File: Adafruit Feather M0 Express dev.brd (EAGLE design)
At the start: 50.8 x 22.9 mm, 41 parts, among them J2 AVR_SPI_PROG_3X2PTH, SW1 SPST_TACT-KMR2, U1 2MB Flash, U2 AP2112-3.3, U3 MCP73831T-2ACI/OT, X1 JSTPH, X2 32.768, X3 microUSB, X4 2x5 0.05" SWD

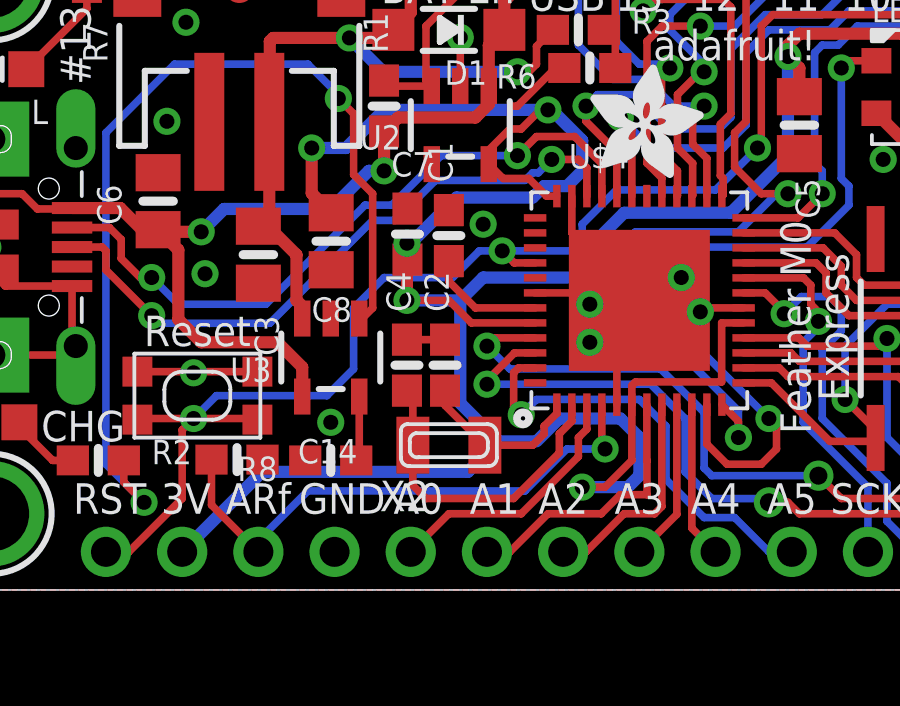
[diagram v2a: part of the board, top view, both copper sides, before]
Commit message: last bad overlap fixed! Still unsure about the bottom layer groundplane under the +3v3 end of C7
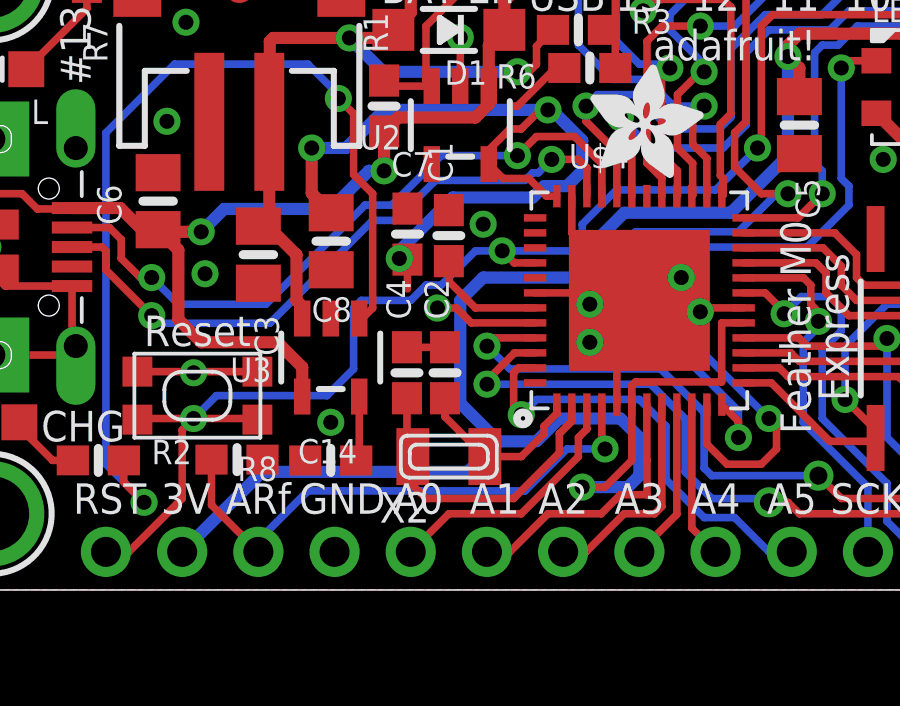
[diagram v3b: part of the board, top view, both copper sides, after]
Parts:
- moved X2 0.38 mm to (17.8, 4.45)
- moved C2 0.25 mm to (17.7, 7.24)
- moved C4 0.25 mm to (16.4, 7.24)
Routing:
- net +3V3: track 150.3 -> 145.9 mm
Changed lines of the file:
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@@
 <attribute name="VALUE" x="18.161" y="10.795" size="0.8128" layer="27" font="vector" ratio="10" rot="R90"/>
 </element>
-<element name="C2" library="microbuilder" package="0603-NO" value="22pF" x="17.653" y="7.493" smashed="yes" rot="R90">
-<attribute name="NAME" x="17.78" y="9.271" size="0.8128" layer="25" font="vector" ratio="18" rot="R90"/>
-<attribute name="VALUE" x="18.034" y="6.477" size="0.8128" layer="27" font="vector" ratio="10" rot="R90"/>
-</element>
-<element name="C4" library="microbuilder" package="0603-NO" value="22pF" x="16.383" y="7.493" smashed="yes" rot="R90">
-<attribute name="NAME" x="16.51" y="9.271" size="0.8128" layer="25" font="vector" ratio="18" rot="R90"/>
-<attribute name="VALUE" x="16.891" y="6.35" size="0.8128" layer="27" font="vector" ratio="10" rot="R90"/>
-</element>
-<element name="X2" library="adafruit2" package="XTAL3215" value="32.768" x="17.78" y="4.826" smashed="yes">
-<attribute name="NAME" x="15.48" y="2.626" size="1.016" layer="25" font="vector"/>
-<attribute name="VALUE" x="15.942" y="4.502" size="0.8128" layer="27" font="vector"/>
+<element name="C2" library="microbuilder" package="0603-NO" value="22pF" x="17.653" y="7.239" smashed="yes" rot="R90">
+<attribute name="NAME" x="17.78" y="9.017" size="0.8128" layer="25" font="vector" ratio="18" rot="R90"/>
+<attribute name="VALUE" x="18.034" y="6.223" size="0.8128" layer="27" font="vector" ratio="10" rot="R90"/>
+</element>
+<element name="C4" library="microbuilder" package="0603-NO" value="22pF" x="16.383" y="7.239" smashed="yes" rot="R90">
+<attribute name="NAME" x="16.51" y="9.017" size="0.8128" layer="25" font="vector" ratio="18" rot="R90"/>
+<attribute name="VALUE" x="16.891" y="6.096" size="0.8128" layer="27" font="vector" ratio="10" rot="R90"/>
+</element>
+<element name="X2" library="adafruit2" package="XTAL3215" value="32.768" x="17.78" y="4.445" smashed="yes">
+<attribute name="NAME" x="15.48" y="2.245" size="1.016" layer="25" font="vector"/>
+<attribute name="VALUE" x="15.942" y="4.121" size="0.8128" layer="27" font="vector"/>
 </element>
 <element name="C5" library="microbuilder" package="0805-NO" value="10uF" x="29.464" y="15.494" smashed="yes" rot="R270">
@@
 <wire x1="23.88" y1="9.902" x2="24.13" y2="9.652" width="0.254" layer="1"/>
 <wire x1="23.38" y1="6.177" x2="23.38" y2="8.902" width="0.254" layer="1"/>
-<wire x1="17.653" y1="8.343" x2="16.383" y2="8.343" width="0.254" layer="1"/>
+<wire x1="17.653" y1="8.089" x2="16.383" y2="8.089" width="0.254" layer="1"/>
 <via x="9.271" y="7.239" extent="1-16" drill="0.5"/>
 <via x="18.923" y="12.192" extent="1-16" drill="0.5"/>
@@
 <wire x1="22.987" y1="3.429" x2="22.225" y2="3.429" width="0.254" layer="1"/>
 <via x="22.225" y="3.429" extent="1-16" drill="0.5"/>
-<via x="16.383" y="9.652" extent="1-16" drill="0.5"/>
+<via x="17.399" y="9.398" extent="1-16" drill="0.5"/>
 <wire x1="21.463" y1="5.715" x2="23.499" y2="5.715" width="0.4064" layer="16"/>
 <wire x1="23.499" y1="5.715" x2="24.13" y2="5.084" width="0.4064" layer="16"/>
@@
 <wire x1="21.209" y1="16.002" x2="22.225" y2="14.986" width="0.4064" layer="16"/>
 <wire x1="16.4" y1="10.0351" x2="16.4" y2="11.012" width="0.254" layer="1"/>
-<wire x1="18.161" y1="9.652" x2="16.51" y2="9.652" width="0.4064" layer="16"/>
 <wire x1="27.605" y1="8.902" x2="26.8732" y2="8.902" width="0.254" layer="1"/>
 <wire x1="26.8732" y1="8.902" x2="26.8732" y2="6.9342" width="0.254" layer="1"/>
@@
 <wire x1="20.193" y1="15.367" x2="20.828" y2="16.002" width="0.254" layer="1"/>
 <wire x1="20.828" y1="16.002" x2="21.082" y2="16.002" width="0.254" layer="1"/>
-<wire x1="16.51" y1="9.652" x2="16.383" y2="9.525" width="0.4064" layer="16"/>
-<wire x1="16.383" y1="9.525" x2="16.383" y2="9.652" width="0.4064" layer="16"/>
-<wire x1="16.383" y1="9.652" x2="16.383" y2="10.995" width="0.4064" layer="1"/>
 <wire x1="27.178" y1="12.573" x2="23.622" y2="12.573" width="0.4064" layer="16"/>
 <wire x1="27.178" y1="12.573" x2="29.083" y2="14.478" width="0.4064" layer="16"/>
@@
 <wire x1="20.447" y1="13.716" x2="19.5889" y2="13.716" width="0.254" layer="1"/>
 <wire x1="19.5889" y1="13.716" x2="19.111" y2="14.1939" width="0.254" layer="1"/>
-<wire x1="20.574" y1="13.081" x2="20.955" y2="13.462" width="0.4064" layer="16"/>
+<wire x1="20.955" y1="13.462" x2="20.574" y2="13.081" width="0.4064" layer="16"/>
 <wire x1="21.717" y1="13.462" x2="20.955" y2="13.462" width="0.4064" layer="16"/>
-<wire x1="16.4" y1="11.012" x2="16.4" y2="11.54" width="0.4064" layer="1"/>
-<wire x1="16.4" y1="11.54" x2="16.383" y2="11.557" width="0.4064" layer="1"/>
-<via x="16.383" y="11.557" extent="1-16" drill="0.5"/>
-<wire x1="16.383" y1="11.557" x2="16.51" y2="11.557" width="0.4064" layer="16"/>
-<wire x1="16.51" y1="11.557" x2="18.034" y2="13.081" width="0.4064" layer="16"/>
-<wire x1="18.034" y1="13.081" x2="20.574" y2="13.081" width="0.4064" layer="16"/>
+<via x="16.129" y="11.049" extent="1-16" drill="0.5"/>
+<wire x1="16.129" y1="11.303" x2="16.129" y2="11.049" width="0.4064" layer="16"/>
 <wire x1="22.606" y1="10.414" x2="18.923" y2="10.414" width="0.4064" layer="16"/>
 <wire x1="18.923" y1="10.414" x2="18.161" y2="9.652" width="0.4064" layer="16"/>
 <wire x1="20.655" y1="8.902" x2="18.53" y2="8.902" width="0.254" layer="1"/>
-<wire x1="18.53" y1="8.902" x2="17.78" y2="9.652" width="0.254" layer="1"/>
-<wire x1="17.78" y1="9.652" x2="16.383" y2="9.652" width="0.254" layer="1"/>
+<wire x1="18.53" y1="8.902" x2="18.034" y2="9.398" width="0.254" layer="1"/>
+<wire x1="18.034" y1="9.398" x2="17.399" y2="9.398" width="0.254" layer="1"/>
 <contactref element="X4" pad="1"/>
 <contactref element="J2" pad="2"/>
@@
 <wire x1="29.464" y1="17.399" x2="29.464" y2="16.444" width="0.4064" layer="1"/>
 <contactref element="R4" pad="2"/>
+<wire x1="17.907" y1="13.081" x2="16.129" y2="11.303" width="0.4064" layer="16"/>
+<wire x1="20.574" y1="13.081" x2="17.907" y2="13.081" width="0.4064" layer="16"/>
 <wire x1="42.418" y1="4.191" x2="42.418" y2="4.003" width="0" layer="19" extent="1-1"/>
 <wire x1="20.701" y1="4.953" x2="20.574" y2="4.953" width="0" layer="19" extent="16-16"/>
+<wire x1="18.034" y1="9.398" x2="18.161" y2="9.652" width="0" layer="19" extent="1-16"/>
+<wire x1="16.4" y1="10.0351" x2="17.399" y2="9.398" width="0" layer="19" extent="1-1"/>
+<wire x1="16.129" y1="11.049" x2="16.4" y2="11.012" width="0" layer="19" extent="1-1"/>
 </signal>
 <signal name="VBUS">
@@
 <wire x1="22.225" y1="12.192" x2="22.225" y2="11.303" width="0.254" layer="16"/>
 <wire x1="22.225" y1="11.303" x2="19.558" y2="11.303" width="0.254" layer="16"/>
-<wire x1="17.907" y1="10.414" x2="15.621" y2="10.414" width="0.254" layer="16"/>
-<wire x1="15.621" y1="10.414" x2="14.605" y2="9.398" width="0.254" layer="16"/>
+<wire x1="14.605" y1="9.398" x2="14.859" y2="9.652" width="0.254" layer="16"/>
 <wire x1="28.067" y1="14.732" x2="26.67" y2="13.335" width="0.254" layer="16"/>
 <via x="28.067" y="14.732" extent="1-16" drill="0.5"/>
@@
 <wire x1="23.368" y1="13.335" x2="22.225" y2="12.192" width="0.254" layer="16"/>
 <wire x1="26.67" y1="13.335" x2="23.368" y2="13.335" width="0.254" layer="16"/>
-<wire x1="18.796" y1="11.303" x2="17.907" y2="10.414" width="0.254" layer="16"/>
-<wire x1="19.558" y1="11.303" x2="18.796" y2="11.303" width="0.254" layer="16"/>
 <wire x1="44.205" y1="13.97" x2="44.205" y2="16.882" width="0.254" layer="1"/>
 <wire x1="44.205" y1="16.882" x2="43.307" y2="17.78" width="0.254" layer="1"/>
+<wire x1="17.526" y1="10.16" x2="18.669" y2="11.303" width="0.254" layer="16"/>
+<wire x1="19.558" y1="11.303" x2="18.669" y2="11.303" width="0.254" layer="16"/>
+<wire x1="14.859" y1="9.652" x2="16.51" y2="9.652" width="0.254" layer="16"/>
+<wire x1="17.018" y1="10.16" x2="17.526" y2="10.16" width="0.254" layer="16"/>
+<wire x1="16.51" y1="9.652" x2="17.018" y2="10.16" width="0.254" layer="16"/>
 </signal>
 <signal name="SWCLK">
@@
 <wire x1="21.38" y1="5.886" x2="20.955" y2="5.461" width="0.254" layer="1"/>
 <wire x1="20.955" y1="5.461" x2="20.955" y2="5.207" width="0.254" layer="1"/>
-<wire x1="20.955" y1="5.207" x2="20.574" y2="4.826" width="0.254" layer="1"/>
-<wire x1="20.574" y1="4.826" x2="18.98" y2="4.826" width="0.254" layer="1"/>
-<wire x1="17.653" y1="6.643" x2="17.653" y2="6.153" width="0.254" layer="1"/>
-<wire x1="17.653" y1="6.153" x2="18.98" y2="4.826" width="0.254" layer="1"/>
+<wire x1="20.955" y1="5.207" x2="20.193" y2="4.445" width="0.254" layer="1"/>
+<wire x1="18.98" y1="4.445" x2="20.193" y2="4.445" width="0.254" layer="1"/>
+<wire x1="17.653" y1="5.772" x2="18.98" y2="4.445" width="0.254" layer="1"/>
+<wire x1="17.653" y1="6.389" x2="17.653" y2="5.772" width="0.254" layer="1"/>
 </signal>
 <signal name="N$7">
@@
 <wire x1="19.939" y1="3.048" x2="21.463" y2="4.572" width="0.254" layer="1"/>
 <wire x1="21.88" y1="5.624" x2="21.88" y2="6.177" width="0.254" layer="1"/>
-<wire x1="16.383" y1="6.643" x2="16.58" y2="6.446" width="0.254" layer="1"/>
-<wire x1="16.58" y1="6.446" x2="16.58" y2="4.826" width="0.254" layer="1"/>
 <wire x1="17.018" y1="3.048" x2="16.58" y2="3.486" width="0.254" layer="1"/>
-<wire x1="16.58" y1="3.486" x2="16.58" y2="4.826" width="0.254" layer="1"/>
+<wire x1="16.58" y1="3.486" x2="16.58" y2="4.445" width="0.254" layer="1"/>
 <wire x1="21.88" y1="5.624" x2="21.463" y2="5.207" width="0.254" layer="1"/>
 <wire x1="21.463" y1="5.207" x2="21.463" y2="4.572" width="0.254" layer="1"/>
+<wire x1="16.383" y1="6.389" x2="16.383" y2="4.572" width="0.254" layer="1"/>
+<wire x1="16.383" y1="4.572" x2="16.58" y2="4.445" width="0" layer="19" extent="1-1"/>
 </signal>
 <signal name="EN">

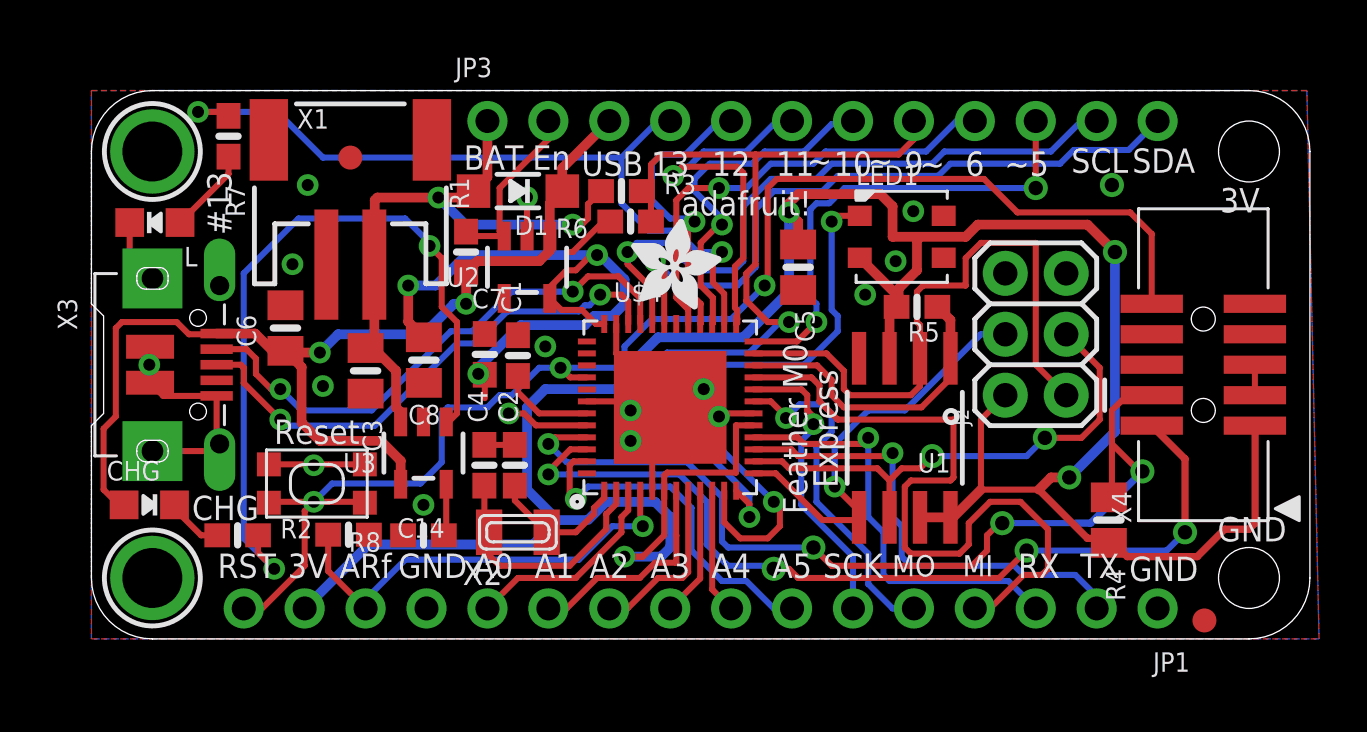
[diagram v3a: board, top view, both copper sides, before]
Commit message: fixed up silkscreen
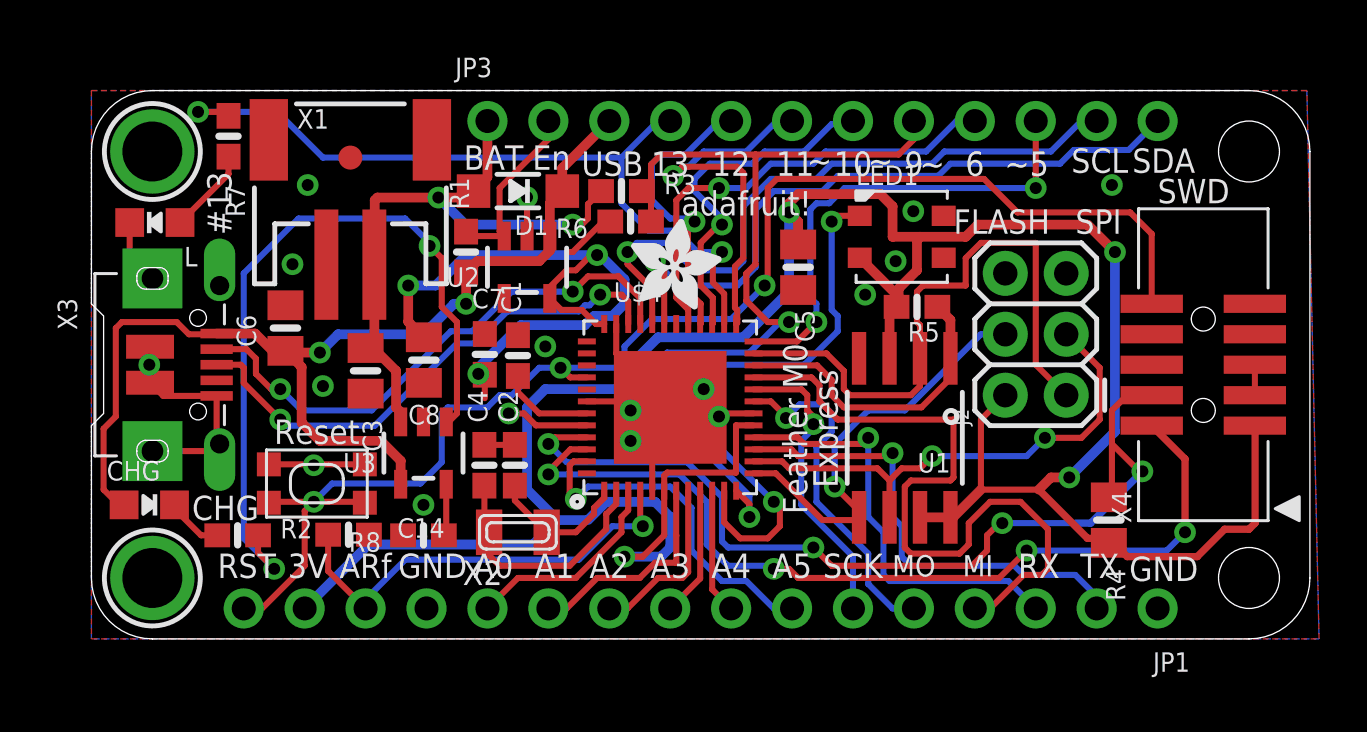
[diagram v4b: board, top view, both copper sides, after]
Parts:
- removed U$35: FIDUCIAL"", microbuilder:FIDUCIAL_1MM
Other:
- board text added: "Developer"
- board text added: "Edition"
- board text added: "FLASH"
- board text added: "SPI"
- board text added: "SWD"
- board text removed: "Feather M0 Express"
- board text removed: "swclk"
- board text removed: "swdio"
